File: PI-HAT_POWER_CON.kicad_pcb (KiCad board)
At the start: 2 copper layers, 15 x 65 mm, 3 parts, among them J101 282834-2, J102 Raspberry_Pi_2x20_PTH_NoSilk

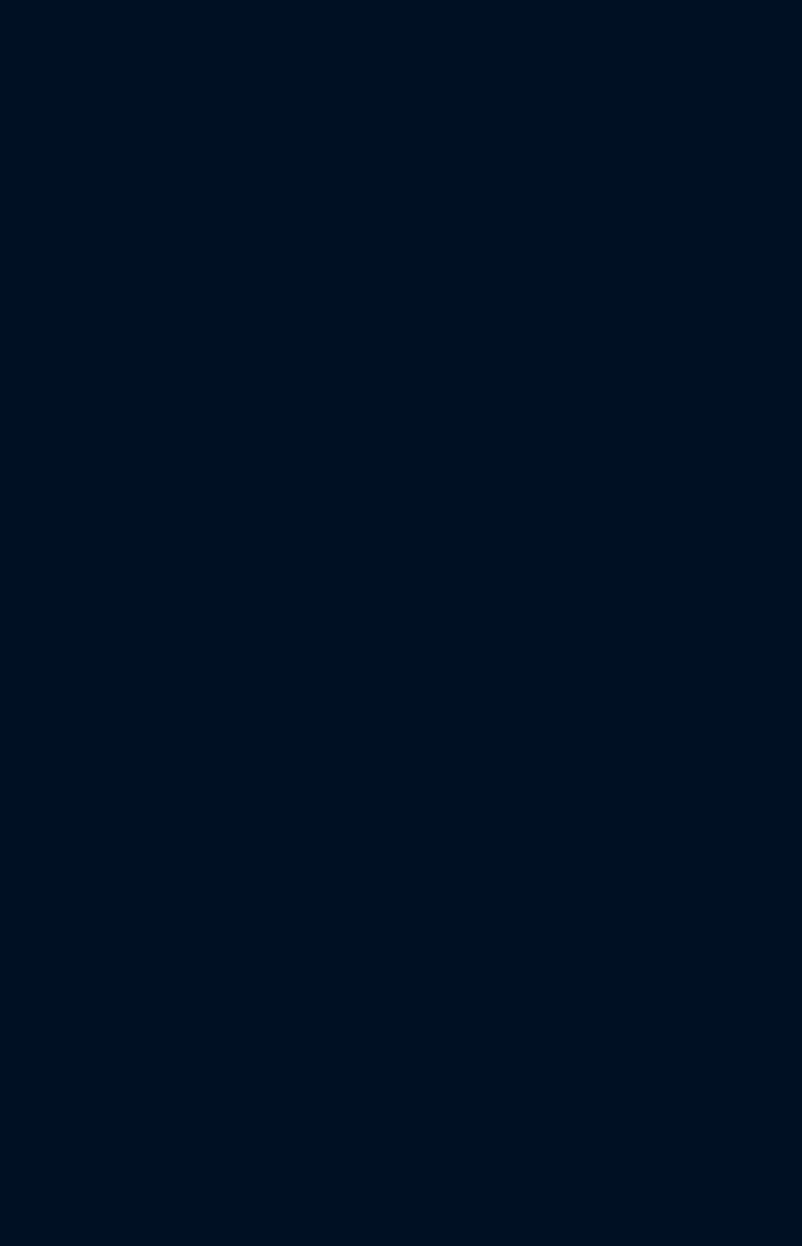
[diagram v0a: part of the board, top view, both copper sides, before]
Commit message: Add M41T0M6 RTC component to project schematic, PCB, and project settings
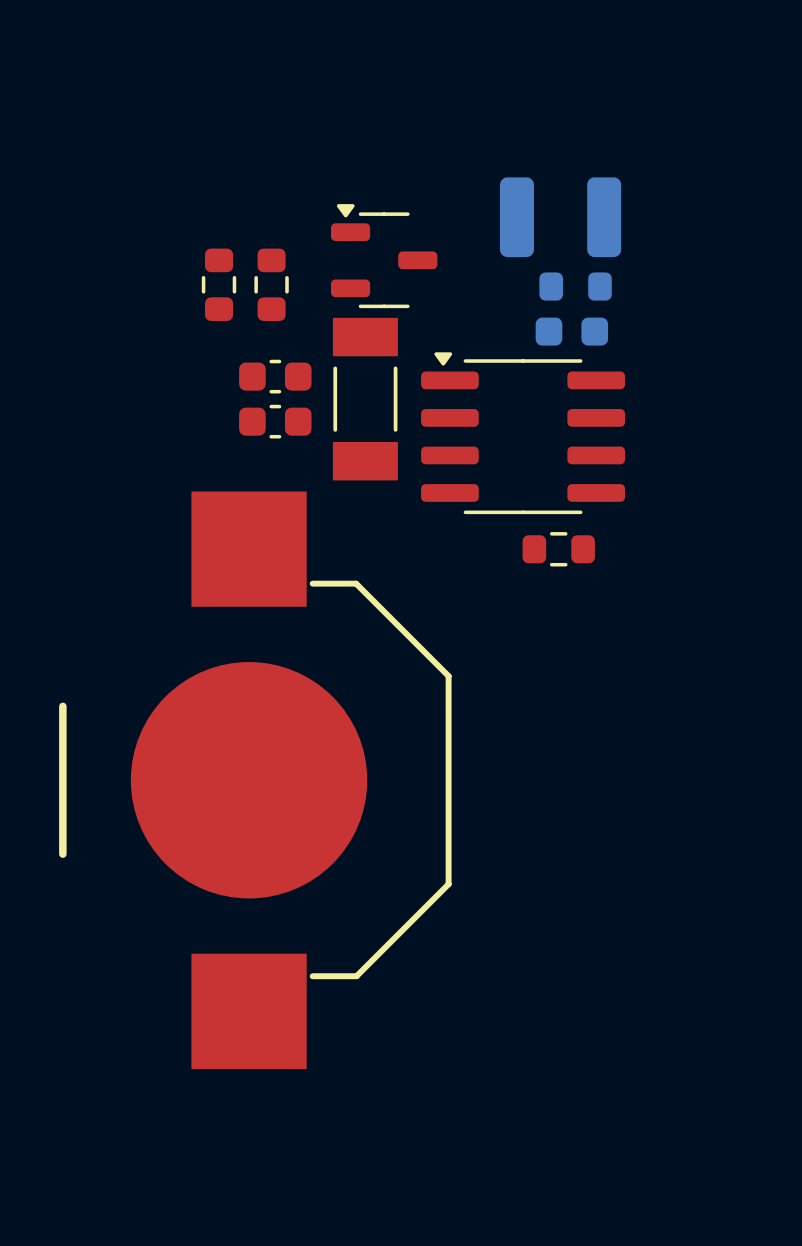
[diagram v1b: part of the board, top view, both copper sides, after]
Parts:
- added BAT1401: Keystone-3000, 0_NORTEK_DIVERS_LOCAL:T_Keystone_3000, F.Cu at (113.2, 142.2)
- added C1401: 100nF, Capacitor_SMD:C_0603_1608Metric, B.Cu at (124.2, 127.1)
- added C1402: 27pF, Capacitor_SMD:C_0603_1608Metric, F.Cu at (114.1, 128.6)
- added C1403: 27pF, Capacitor_SMD:C_0603_1608Metric, F.Cu at (114.1, 130.1)
- added C1404: 22uF, Capacitor_SMD:C_1210_3225Metric, B.Cu at (123.8, 123.2)
- added D1401: BAT54C-7-F, Package_TO_SOT_SMD:SOT-23-3, F.Cu at (117.8, 124.7)
- added IC1401: M41T0M6, Package_SO:SOIC-8_3.9x4.9mm_P1.27mm, F.Cu at (122.5, 130.6)
- added OSC1401: CC4V-T1A, 0_NORTEK_GLOBAL:T_MC_CC4V-T1A, F.Cu at (117.2, 129.4)
- added R1401: 100K, Resistor_SMD:R_0603_1608Metric, F.Cu at (123.7, 134.4)
- added R1402: 0R, Resistor_SMD:R_0603_1608Metric, B.Cu at (124.3, 125.5)
- added R1403: 22R, Resistor_SMD:R_0603_1608Metric, F.Cu at (114.0, 125.5)
- added R1404: 22R, Resistor_SMD:R_0603_1608Metric, F.Cu at (112.2, 125.5)

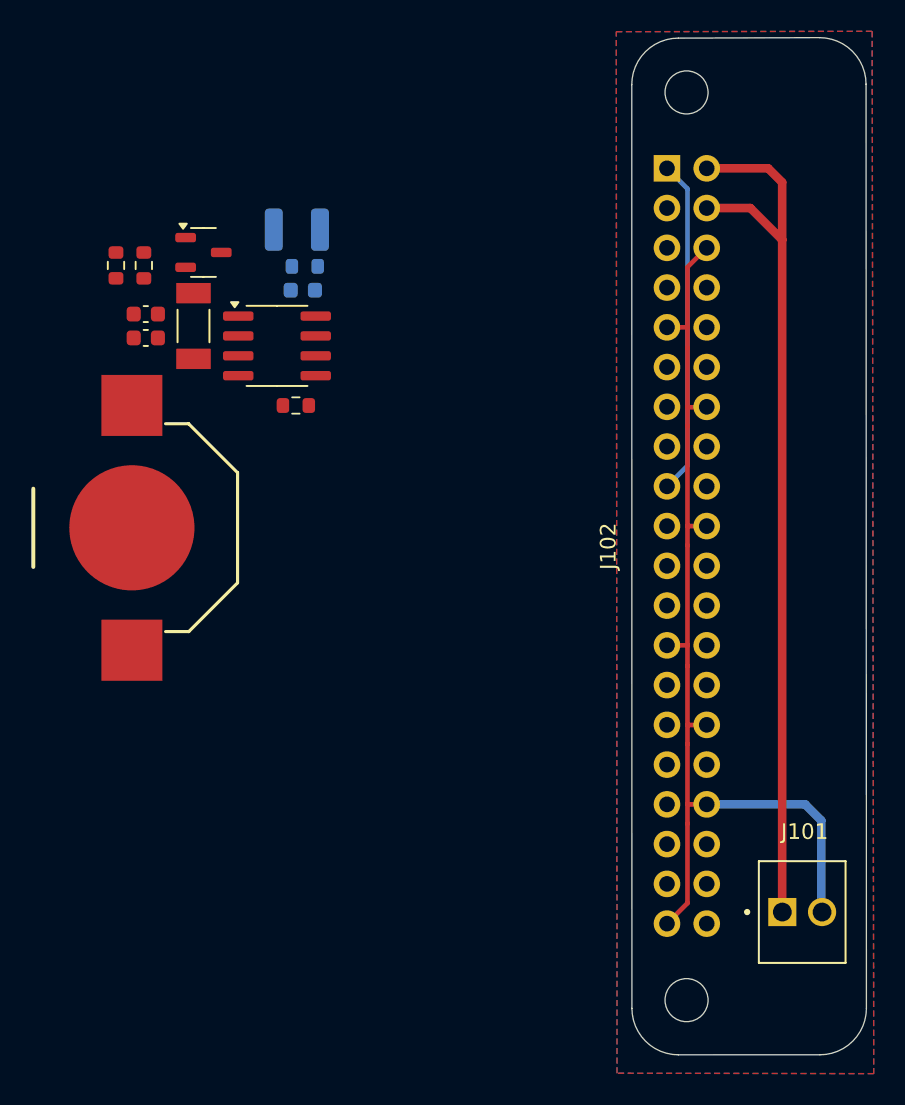
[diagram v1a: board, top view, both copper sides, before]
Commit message: Route PCB: Complete all nets, DRC clear, power and RTC connectivity verified
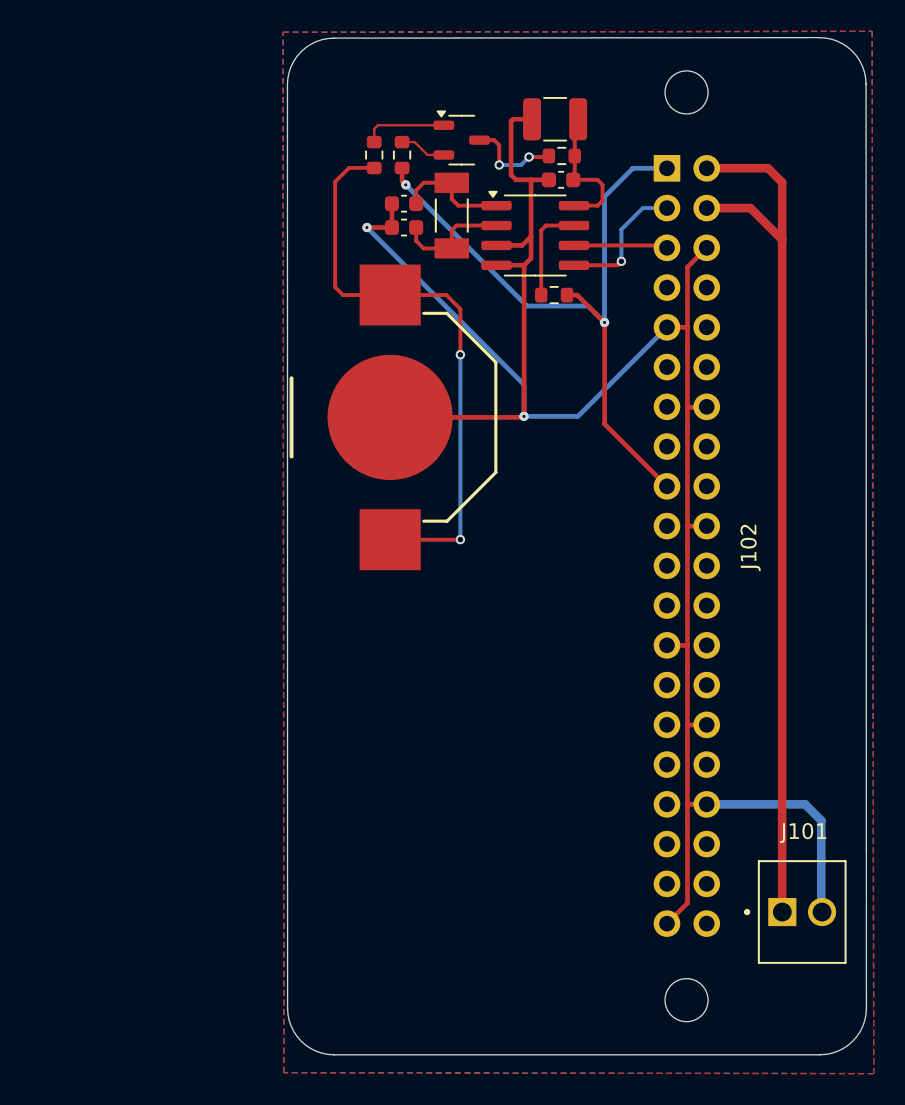
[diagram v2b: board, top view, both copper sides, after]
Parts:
- removed ?: , clipboard:85326a09-dce3-4476-a840-32de8478bbeb
- C1401, C1404, R1402: moved to F.Cu
- moved D1401 18.0 mm to (134.3, 117.5)
- moved IC1401 17.9 mm to (139.0, 123.6)
- moved R1401 17.9 mm to (140.2, 127.4)
- moved R1404 17.9 mm to (128.7, 118.4)
- moved C1402 17.9 mm to (130.6, 121.5)
- moved C1403 17.9 mm to (130.6, 123.1)
- moved OSC1401 17.9 mm to (133.7, 122.3)
- moved BAT1401 17.9 mm to (129.8, 135.2)
- moved C1401 17.9 mm to (140.7, 120.0)
- moved C1404 17.9 mm to (140.3, 116.1)
- moved R1403 17.9 mm to (130.5, 118.4)
- moved R1402 17.9 mm to (140.7, 118.5)
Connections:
- net /Viola/EXTERNAL_RTC/VCC_BATTERY renamed /VCC_BATTERY
- net /Viola/EXTERNAL_RTC/VCC_RTC renamed /VCC_RTC
- IC1401 pad 5: /ProtectionCunsumption/I2C.SDA -> /I2C.SDA
- IC1401 pad 6: /ProtectionCunsumption/I2C.SCL -> /I2C.SCL
- J102 pad 1: Net-(J102-3V3-Pad1) -> +3V3
- J102 pad 17: Net-(J102-3V3-Pad1) -> +3V3
- J102 pad 3: unconnected-(J102-SDA/GPIO2-Pad3) -> /I2C.SDA
- J102 pad 5: unconnected-(J102-SCL/GPIO3-Pad5) -> /I2C.SCL
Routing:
- net GND: track 65.2 -> 131.5 mm, vias 0 -> 2
- net +3V3: track 0.00 -> 45.5 mm, vias 0 -> 2
- net /VCC_BATTERY: track 0.00 -> 37.4 mm, vias 0 -> 2
- net Net-(J102-3V3-Pad1): track 21.4 -> 0.00 mm
- net /VCC_RTC: track 0.00 -> 8.98 mm
- net /I2C.SDA: track 0.00 -> 8.65 mm, vias 0 -> 1
- net Net-(IC1401-OSCO): track 0.00 -> 7.49 mm
- net Net-(IC1401-OSCI): track 0.00 -> 7.40 mm
- net Net-(IC1401-OUT): track 0.00 -> 6.36 mm
- net VCC_BAT: track 0.00 -> 6.08 mm, vias 0 -> 2
- net /I2C.SCL: track 0.00 -> 6.01 mm
- net Net-(D1401-Pad1): track 0.00 -> 5.39 mm
- net Net-(D1401-Pad2): track 0.00 -> 3.01 mm
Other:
- board size 15 x 65 mm -> 37 x 65 mm

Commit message: prepare for v300326 production
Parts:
- added G***: LOGO, 0_NORTEK_GLOBAL:LOGO-NORTEK_small, F.Cu at (134.2, 163.2)
- J101: value 282834-2 -> ${REVISION}
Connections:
- net Net-(J101-Pin_1) renamed +5.1V
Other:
- board text added: "${TITLE}"
